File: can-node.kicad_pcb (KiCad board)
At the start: 2 copper layers, 68.6 x 66.8 mm, 36 parts, among them J1 Conn_01x02_Pin, J10 MCP2551, J11 Conn_01x02_Socket, J13 SDA, J14 SCL, J15 MD13 SIGNAL, J17 MD13S PWR, J2 Conn_01x02_Pin, J3 CAN, J4 CAN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

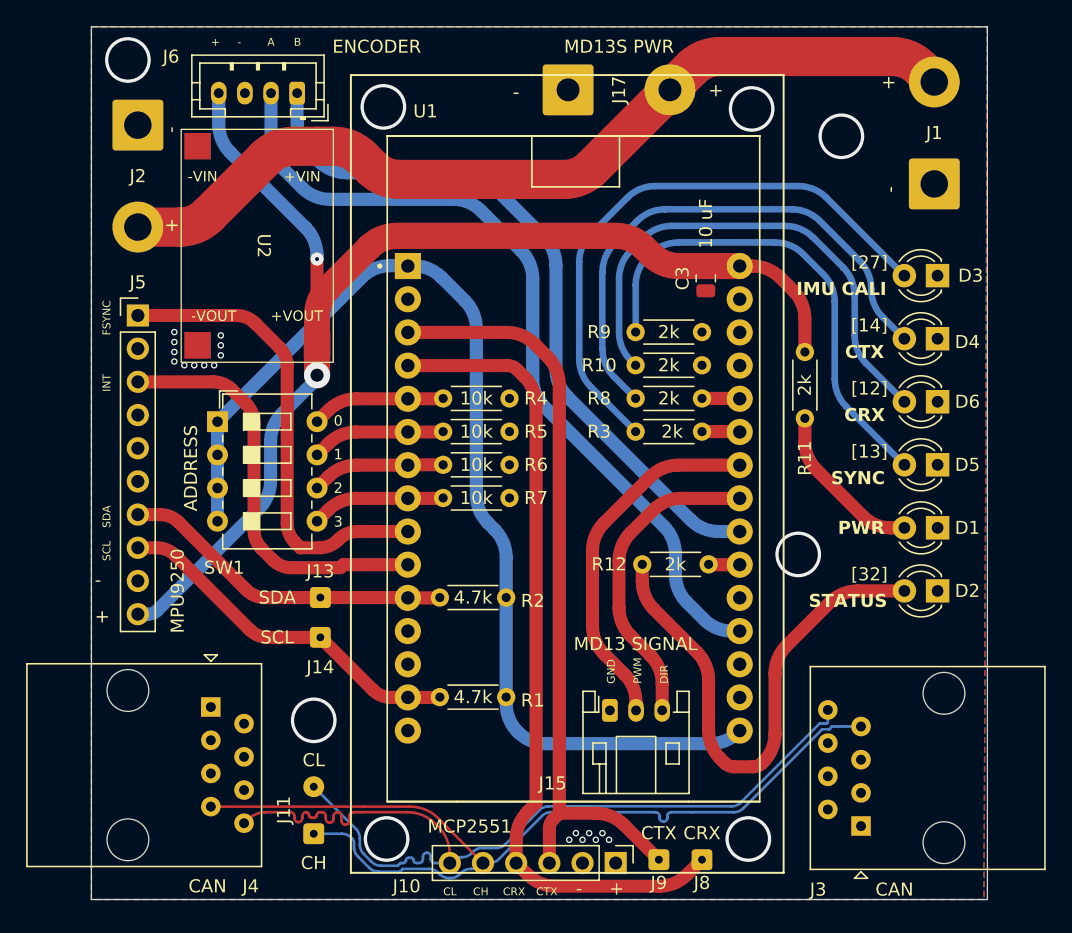
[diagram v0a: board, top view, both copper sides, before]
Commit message: fix 5V for MCP
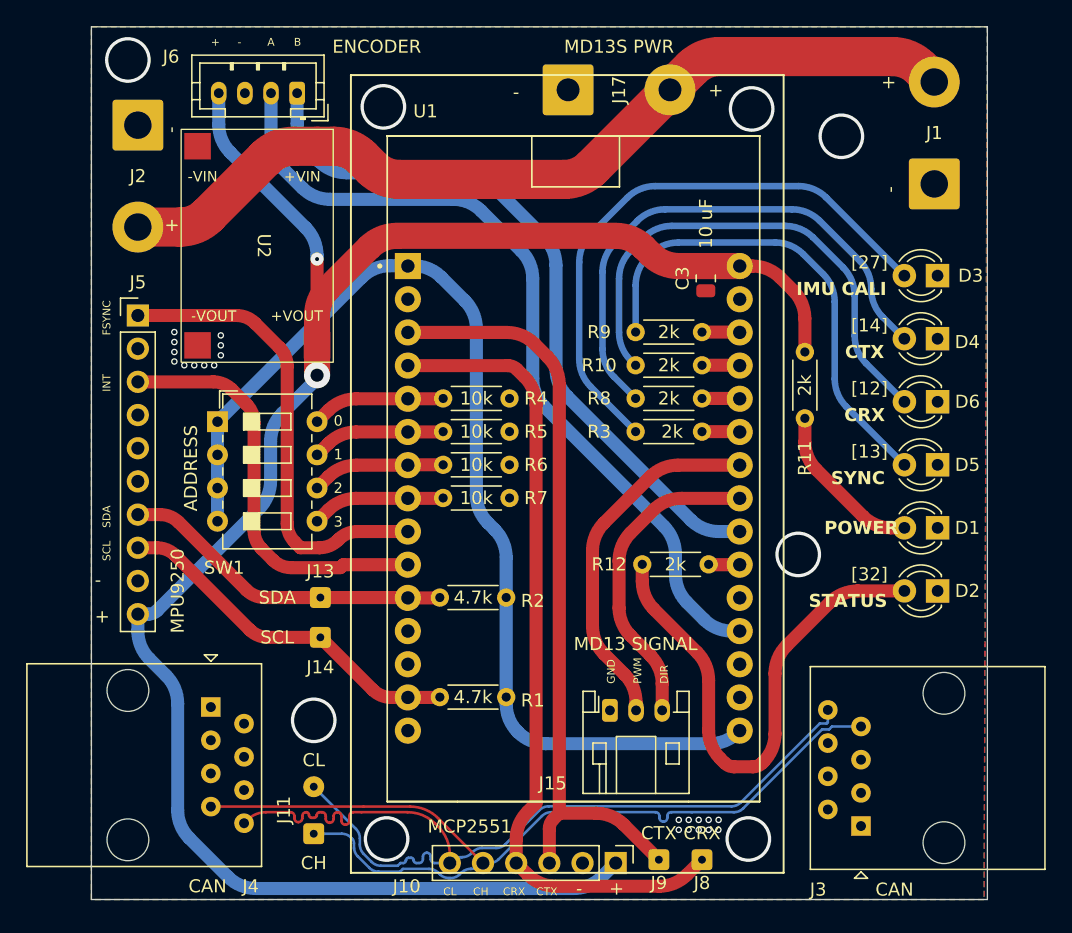
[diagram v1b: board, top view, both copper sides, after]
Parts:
- D1: value PWR -> POWER
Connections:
- J10 pad 1: +5VA -> +5V
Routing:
- net +5V: track 96.4 -> 149.5 mm
- net LED1: track 0.00 -> 2.90 mm
- net LED0: track 0.00 -> 2.90 mm
- net GND: vias 18 -> 21

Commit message: add 5V
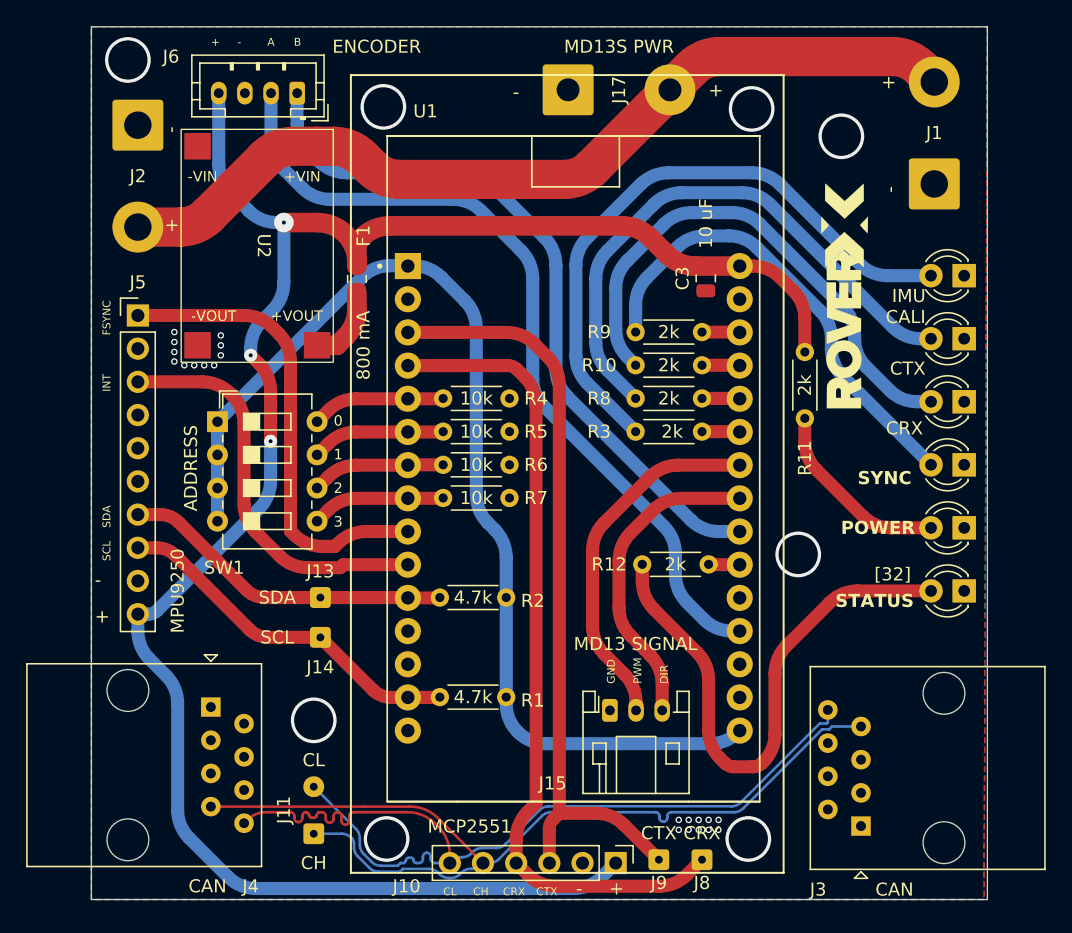
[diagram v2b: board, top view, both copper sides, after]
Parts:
- added F1: 800 mA, Fuse:Fuse_0805_2012Metric_Pad1.15x1.40mm_HandSolder, F.Cu at (103.4, 60.2)
- moved D1 2.04 mm to (149.9, 79.2)
- moved D2 2.04 mm to (149.9, 84.1)
- moved D3 2.04 mm to (149.9, 59.9)
- moved D4 2.04 mm to (149.9, 64.8)
- moved D5 2.04 mm to (149.9, 74.4)
- moved D6 2.04 mm to (149.9, 69.6)
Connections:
- U2 pad 3: +5V -> Net-(U2-V_OUT)
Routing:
- net Net-(U2-V_OUT): track 0.00 -> 6.08 mm
- net Net-(D3-A): track 45.1 -> 48.0 mm
- net Net-(D4-A): track 41.3 -> 43.4 mm
- net Net-(D2-A): track 40.5 -> 42.5 mm
- net Net-(D1-A): track 12.6 -> 14.6 mm
- net +5V: track 149.5 -> 151.3 mm, vias 2 -> 3
- net Net-(D5-A): track 37.5 -> 36.1 mm
- net Net-(D6-A): track 39.4 -> 40.4 mm
- net INT: track 32.1 -> 31.2 mm
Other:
- board text added: "IMU CALI"
- board text removed: "[12]"
- board text removed: "[13]"
- board text removed: "[14]"
- board text removed: "[27]"

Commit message: clean up silkscreen
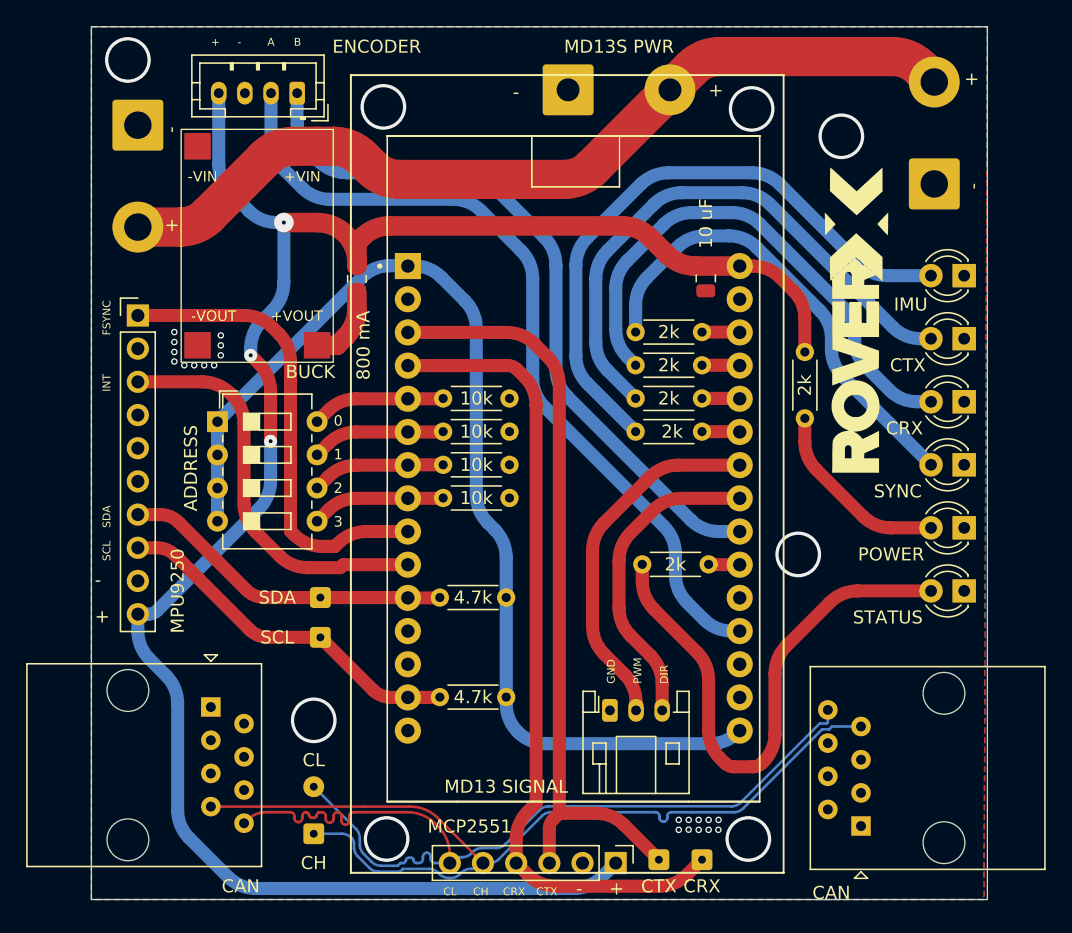
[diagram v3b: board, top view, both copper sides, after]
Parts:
- U2: value ~ -> BUCK
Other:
- board text added: "IMU"
- board text removed: "IMU CALI"
- board text removed: "[32]"

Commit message: rm i2c pull-ups
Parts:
- removed R1, R2: 4.7k, Resistor_THT:R_Axial_DIN0204_L3.6mm_D1.6mm_P5.08mm_Horizontal
- U2: value BUCK -> ~
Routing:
- net I2C-SDA: track 25.6 -> 23.1 mm
- net I2C-SCL: track 27.6 -> 25.1 mm
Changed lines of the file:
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@@
     )
   )
-  (footprint "Resistor_THT:R_Axial_DIN0204_L3.6mm_D1.6mm_P5.08mm_Horizontal" (layer "F.Cu")
-    (at 114.808 92.202 180)
-    (descr "Resistor, Axial_DIN0204 series, Axial, Horizontal, pin pitch=5.08mm, 0.167W, length*diameter=3.6*1.6mm^2, http://cdn-reichelt.de/documents/datenblatt/B400/1_4W%23YAG.pdf")
-    (tags "Resistor Axial_DIN0204 series Axial Horizontal pin pitch 5.08mm 0.167W length 3.6mm diameter 1.6mm")
-    (property "Sheetfile" "can-node.kicad_sch")
-    (property "Sheetname" "")
-    (property "ki_description" "Resistor")
-    (property "ki_keywords" "R res resistor")
-    (attr through_hole)
-    (fp_text reference "R1" (at -2.032 -0.254 180) (layer "F.SilkS") hide
-        (effects (font (size 1 1) (thickness 0.15)))
-    )
-    (fp_text value "4.7k" (at 2.54 0 180) (layer "F.SilkS")
-        (effects (font (size 1 1) (thickness 0.15)))
-    )
-    (fp_text user "${REFERENCE}" (at 2.54 0 180) (layer "F.Fab")
-        (effects (font (size 0.72 0.72) (thickness 0.108)))
-    )
-    (fp_line (start 0.62 -0.92) (end 4.46 -0.92)
-      (stroke (width 0.12) (type solid)) (layer "F.SilkS"))
-    (fp_line (start 0.62 0.92) (end 4.46 0.92)
-      (stroke (width 0.12) (type solid)) (layer "F.SilkS"))
-    (fp_line (start -0.95 -1.05) (end -0.95 1.05)
-      (stroke (width 0.05) (type solid)) (layer "F.CrtYd"))
-    (fp_line (start -0.95 1.05) (end 6.03 1.05)
-      (stroke (width 0.05) (type solid)) (layer "F.CrtYd"))
-    (fp_line (start 6.03 -1.05) (end -0.95 -1.05)
-      (stroke (width 0.05) (type solid)) (layer "F.CrtYd"))
-    (fp_line (start 6.03 1.05) (end 6.03 -1.05)
-      (stroke (width 0.05) (type solid)) (layer "F.CrtYd"))
-    (fp_line (start 0 0) (end 0.74 0)
-      (stroke (width 0.1) (type solid)) (layer "F.Fab"))
-    (fp_line (start 0.74 -0.8) (end 0.74 0.8)
-      (stroke (width 0.1) (type solid)) (layer "F.Fab"))
-    (fp_line (start 0.74 0.8) (end 4.34 0.8)
-      (stroke (width 0.1) (type solid)) (layer "F.Fab"))
-    (fp_line (start 4.34 -0.8) (end 0.74 -0.8)
-      (stroke (width 0.1) (type solid)) (layer "F.Fab"))
-    (fp_line (start 4.34 0.8) (end 4.34 -0.8)
-      (stroke (width 0.1) (type solid)) (layer "F.Fab"))
-    (fp_line (start 5.08 0) (end 4.34 0)
-      (stroke (width 0.1) (type solid)) (layer "F.Fab"))
-    (pad "1" thru_hole circle (at 0 0 180) (size 1.4 1.4) (drill 0.7) (layers "*.Cu" "*.Mask")
-      (net 34 "+3.3V") (pintype "passive"))
-    (pad "2" thru_hole oval (at 5.08 0 180) (size 1.4 1.4) (drill 0.7) (layers "*.Cu" "*.Mask")
-      (net 27 "I2C-SCL") (pintype "passive"))
-    (model "${KICAD6_3DMODEL_DIR}/Resistor_THT.3dshapes/R_Axial_DIN0204_L3.6mm_D1.6mm_P5.08mm_Horizontal.wrl"
-      (offset (xyz 0 0 0))
-      (scale (xyz 1 1 1))
-      (rotate (xyz 0 0 0))
-    )
-  )
   (footprint "Connector_Wire:SolderWire-1.5sqmm_1x02_P7.8mm_D1.7mm_OD3.9mm" (layer "F.Cu")
     (at 86.614 48.424 -90)
@@
     (fp_line (start 1 0.6) (end -1 0.6)
       (stroke (width 0.1) (type solid)) (layer "F.Fab"))
-    (pad "1" smd roundrect (at -1.025 0 90) (size 1.15 1.4) (layers "F.Cu" "F.Paste" "F.Mask") (roundrect_rratio 0.217391)
+    (pad "1" smd roundrect (at -1.025 0 90) (size 1.15 1.4) (layers "F.Cu" "F.Paste" "F.Mask") (roundrect_rratio 0.2173913043)
       (net 50 "Net-(U2-V_OUT)") (pintype "passive"))
-    (pad "2" smd roundrect (at 1.025 0 90) (size 1.15 1.4) (layers "F.Cu" "F.Paste" "F.Mask") (roundrect_rratio 0.217391)
+    (pad "2" smd roundrect (at 1.025 0 90) (size 1.15 1.4) (layers "F.Cu" "F.Paste" "F.Mask") (roundrect_rratio 0.2173913043)
       (net 1 "+5V") (pintype "passive"))
     (model "${KICAD6_3DMODEL_DIR}/Fuse.3dshapes/Fuse_0805_2012Metric.wrl"
@@
         (effects (font (size 1 1) (thickness 0.1)))
     )
-    (fp_text value "BUCK" (at 9.652 -4.064 unlocked) (layer "F.SilkS")
+    (fp_text value "~" (at 9.652 -4.064 unlocked) (layer "F.SilkS")
         (effects (font (size 1 1) (thickness 0.15)))
     )
@@
     )
   )
-  (footprint "Resistor_THT:R_Axial_DIN0204_L3.6mm_D1.6mm_P5.08mm_Horizontal" (layer "F.Cu")
-    (at 114.808 84.582 180)
-    (descr "Resistor, Axial_DIN0204 series, Axial, Horizontal, pin pitch=5.08mm, 0.167W, length*diameter=3.6*1.6mm^2, http://cdn-reichelt.de/documents/datenblatt/B400/1_4W%23YAG.pdf")
-    (tags "Resistor Axial_DIN0204 series Axial Horizontal pin pitch 5.08mm 0.167W length 3.6mm diameter 1.6mm")
-    (property "Sheetfile" "can-node.kicad_sch")
-    (property "Sheetname" "")
-    (property "ki_description" "Resistor")
-    (property "ki_keywords" "R res resistor")
-    (attr through_hole)
-    (fp_text reference "R2" (at -2.032 -0.254 180) (layer "F.SilkS") hide
-        (effects (font (size 1 1) (thickness 0.15)))
-    )
-    (fp_text value "4.7k" (at 2.54 0 180) (layer "F.SilkS")
-        (effects (font (size 1 1) (thickness 0.15)))
-    )
-    (fp_text user "${REFERENCE}" (at 2.54 0 180) (layer "F.Fab")
-        (effects (font (size 0.72 0.72) (thickness 0.108)))
-    )
-    (fp_line (start 0.62 -0.92) (end 4.46 -0.92)
-      (stroke (width 0.12) (type solid)) (layer "F.SilkS"))
-    (fp_line (start 0.62 0.92) (end 4.46 0.92)
-      (stroke (width 0.12) (type solid)) (layer "F.SilkS"))
-    (fp_line (start -0.95 -1.05) (end -0.95 1.05)
-      (stroke (width 0.05) (type solid)) (layer "F.CrtYd"))
-    (fp_line (start -0.95 1.05) (end 6.03 1.05)
-      (stroke (width 0.05) (type solid)) (layer "F.CrtYd"))
-    (fp_line (start 6.03 -1.05) (end -0.95 -1.05)
-      (stroke (width 0.05) (type solid)) (layer "F.CrtYd"))
-    (fp_line (start 6.03 1.05) (end 6.03 -1.05)
-      (stroke (width 0.05) (type solid)) (layer "F.CrtYd"))
-    (fp_line (start 0 0) (end 0.74 0)
-      (stroke (width 0.1) (type solid)) (layer "F.Fab"))
-    (fp_line (start 0.74 -0.8) (end 0.74 0.8)
-      (stroke (width 0.1) (type solid)) (layer "F.Fab"))
-    (fp_line (start 0.74 0.8) (end 4.34 0.8)
-      (stroke (width 0.1) (type solid)) (layer "F.Fab"))
-    (fp_line (start 4.34 -0.8) (end 0.74 -0.8)
-      (stroke (width 0.1) (type solid)) (layer "F.Fab"))
-    (fp_line (start 4.34 0.8) (end 4.34 -0.8)
-      (stroke (width 0.1) (type solid)) (layer "F.Fab"))
-    (fp_line (start 5.08 0) (end 4.34 0)
-      (stroke (width 0.1) (type solid)) (layer "F.Fab"))
-    (pad "1" thru_hole circle (at 0 0 180) (size 1.4 1.4) (drill 0.7) (layers "*.Cu" "*.Mask")
-      (net 34 "+3.3V") (pintype "passive"))
-    (pad "2" thru_hole oval (at 5.08 0 180) (size 1.4 1.4) (drill 0.7) (layers "*.Cu" "*.Mask")
-      (net 26 "I2C-SDA") (pintype "passive"))
-    (model "${KICAD6_3DMODEL_DIR}/Resistor_THT.3dshapes/R_Axial_DIN0204_L3.6mm_D1.6mm_P5.08mm_Horizontal.wrl"
-      (offset (xyz 0 0 0))
-      (scale (xyz 1 1 1))
-      (rotate (xyz 0 0 0))
-    )
-  )
   (gr_poly
     (pts
@@
   (segment (start 107.255 84.582) (end 107.281 84.608) (width 1) (layer "F.Cu") (net 26))
   (segment (start 100.584 84.582) (end 107.255 84.582) (width 1) (layer "F.Cu") (net 26))
-  (segment (start 109.702 84.608) (end 109.728 84.582) (width 1) (layer "F.Cu") (net 26))
-  (segment (start 107.281 84.608) (end 109.702 84.608) (width 1) (layer "F.Cu") (net 26))
   (segment (start 94.918213 83.996213) (end 89.739786 78.817786) (width 1) (layer "F.Cu") (net 26))
   (segment (start 88.325573 78.232) (end 86.614 78.232) (width 1) (layer "F.Cu") (net 26))
@@
   (arc (start 96.332427 84.582) (mid 95.56706 84.429759) (end 94.918213 83.996213) (width 1) (layer "F.Cu") (net 26))
   (segment (start 104.596213 91.642213) (end 100.584 87.63) (width 1) (layer "F.Cu") (net 27))
-  (segment (start 107.281 92.228) (end 109.702 92.228) (width 1) (layer "F.Cu") (net 27))
   (segment (start 100.584 87.63) (end 96.586427 87.63) (width 1) (layer "F.Cu") (net 27))
-  (segment (start 109.702 92.228) (end 109.728 92.202) (width 1) (layer "F.Cu") (net 27))
   (segment (start 95.172213 87.044213) (end 89.485786 81.357786) (width 1) (layer "F.Cu") (net 27))
   (segment (start 107.281 92.228) (end 106.010427 92.228) (width 1) (layer "F.Cu") (net 27))

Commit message: .
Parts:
- added REF**: MountingHole_3.5mm_Pad, MountingHole:MountingHole_3.5mm_Pad, F.Cu at (86.4, 43.9)
- added REF**: MountingHole_3.5mm_Pad, MountingHole:MountingHole_3.5mm_Pad, F.Cu at (138.4, 80.5)
- added REF**: MountingHole_3.5mm_Pad, MountingHole:MountingHole_3.5mm_Pad, F.Cu at (99.8, 92.7)
- added REF**: MountingHole_3.5mm_Pad, MountingHole:MountingHole_3.5mm_Pad, F.Cu at (133.3, 102.8)
- added REF**: MountingHole_3.5mm_Pad, MountingHole:MountingHole_3.5mm_Pad, F.Cu at (140.5, 48.3)
- added REF**: MountingHole_3.5mm_Pad, MountingHole:MountingHole_3.5mm_Pad, F.Cu at (133.6, 46.9)
- added REF**: MountingHole_3.5mm_Pad, MountingHole:MountingHole_3.5mm_Pad, F.Cu at (105.4, 46.7)
- added REF**: MountingHole_3.5mm_Pad, MountingHole:MountingHole_3.5mm_Pad, F.Cu at (105.7, 102.8)
- moved J2 1.02 mm to (86.6, 49.4)
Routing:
- net CAN-: track 71.4 -> 72.4 mm
- net (no net): vias 8 -> 0
